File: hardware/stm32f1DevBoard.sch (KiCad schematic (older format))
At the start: 33 parts, among them J1 USB_2, M1 Mounting Hole, M2 Mounting Hole, M3 Mounting Hole, M4 Mounting Hole, P1 JTAG, P2 P20, P3 P20, U1 STM32F102C6, X1 32,768Hz, X2 20MHz

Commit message: using kicadcloud files
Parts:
- C1, C10, C2, C3, C4, C5, C6, C7, C8, C9: symbol CSMALL -> CPsmall
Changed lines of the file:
@@
-EESchema Schematic File Version 2  date Wed 19 Dec 2012 11:05:56 PM EST
-LIBS:stm32f1DevBoard
+EESchema Schematic File Version 2  date Wed 02 Jan 2013 12:15:05 PM EST
+LIBS:userFavorites
 LIBS:power
-LIBS:device
-LIBS:transistors
-LIBS:conn
-LIBS:linear
-LIBS:regul
-LIBS:74xx
-LIBS:cmos4000
-LIBS:adc-dac
-LIBS:memory
-LIBS:xilinx
-LIBS:special
-LIBS:microcontrollers
-LIBS:dsp
-LIBS:microchip
-LIBS:analog_switches
-LIBS:motorola
-LIBS:texas
-LIBS:intel
-LIBS:audio
-LIBS:interface
-LIBS:digital-audio
-LIBS:philips
-LIBS:display
-LIBS:cypress
-LIBS:siliconi
-LIBS:opto
-LIBS:atmel
-LIBS:contrib
-LIBS:valves
-LIBS:stm32f1DevBoard-cache
 EELAYER 27 0
 EELAYER END
@@
 $EndComp
 $Comp
-L CSMALL C10
+L CPsmall C10
 U 1 1 50C94FDC
 P 3900 1750
@@
 $EndComp
 $Comp
-L CSMALL C6
+L CPsmall C6
 U 1 1 50C94FE2
 P 3700 1750
@@
 $EndComp
 $Comp
-L CSMALL C5
+L CPsmall C5
 U 1 1 50C94FE8
 P 3500 1750
@@
 $EndComp
 $Comp
-L CSMALL C2
+L CPsmall C2
 U 1 1 50C94FEE
 P 3300 1750
@@
 $EndComp
 $Comp
-L CSMALL C8
+L CPsmall C8
 U 1 1 50C9642F
 P 3800 2550
@@
 $EndComp
 $Comp
-L CSMALL C3
+L CPsmall C3
 U 1 1 50C96435
 P 3300 2550
@@
 $EndComp
 $Comp
-L CSMALL C9
+L CPsmall C9
 U 1 1 50C9643B
 P 3800 3050
@@
 $EndComp
 $Comp
-L CSMALL C4
+L CPsmall C4
 U 1 1 50C9644B
 P 3300 3050
@@
 $EndComp
 $Comp
-L CSMALL C7
+L CPsmall C7
 U 1 1 50CA0DBA
 P 3750 4250
@@
 $EndComp
 $Comp
-L CSMALL C1
+L CPsmall C1
 U 1 1 50CBFE42
 P 3100 1750

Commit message: updates to schematic
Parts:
- X2: value 20MHz -> 8MHz
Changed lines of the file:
@@
-EESchema Schematic File Version 2  date Thu 17 Jan 2013 09:41:47 PM EST
+EESchema Schematic File Version 2  date Mon 21 Jan 2013 10:28:50 PM EST
 LIBS:userFavorites
 LIBS:power
+LIBS:stm32f1DevBoard-cache
 EELAYER 27 0
 EELAYER END
@@
 Sheet 1 4
 Title ""
-Date "18 jan 2013"
+Date "22 jan 2013"
 Rev ""
 Comp ""
@@
 P 3550 2900
 F 0 "X2" H 3550 3025 60  0000 C CNN
-F 1 "20MHz" H 3550 2775 60  0000 C CNN
+F 1 "8MHz" H 3550 2775 60  0000 C CNN
 	1    3550 2900
 	1    0    0    -1

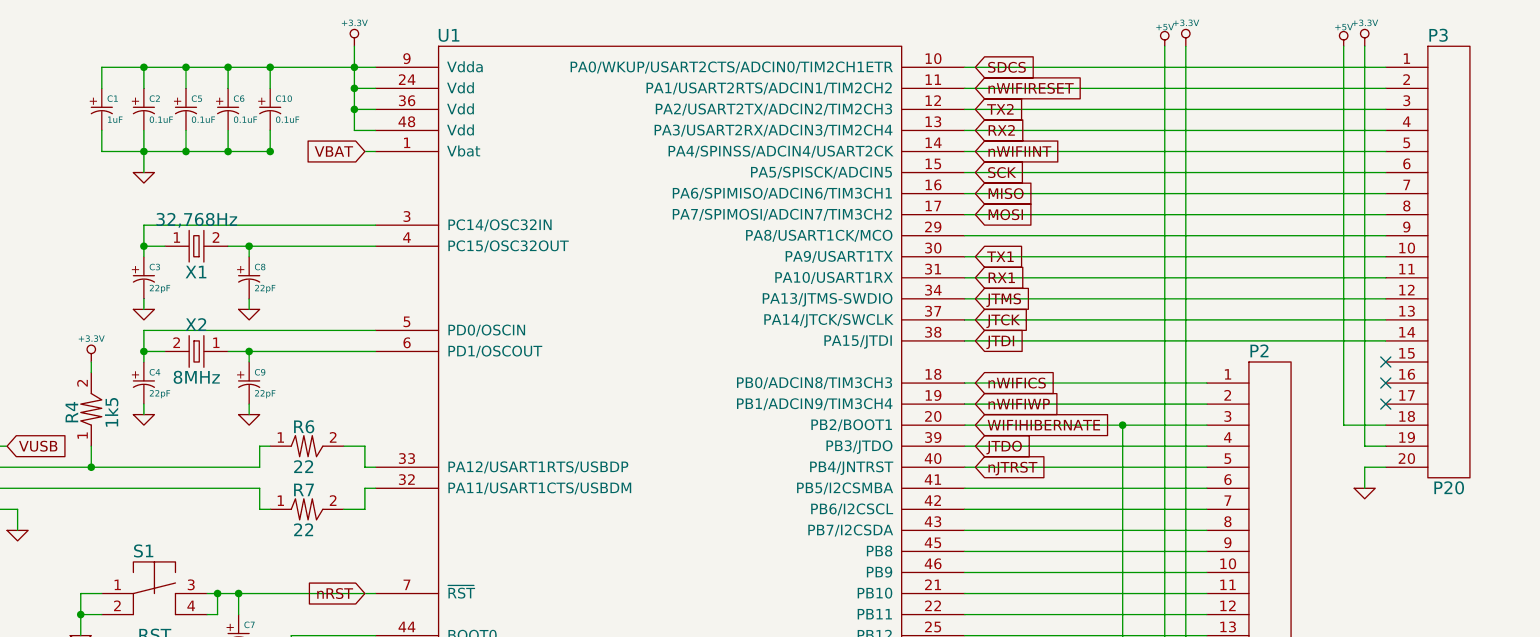
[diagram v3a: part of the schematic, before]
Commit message: fix sdcard
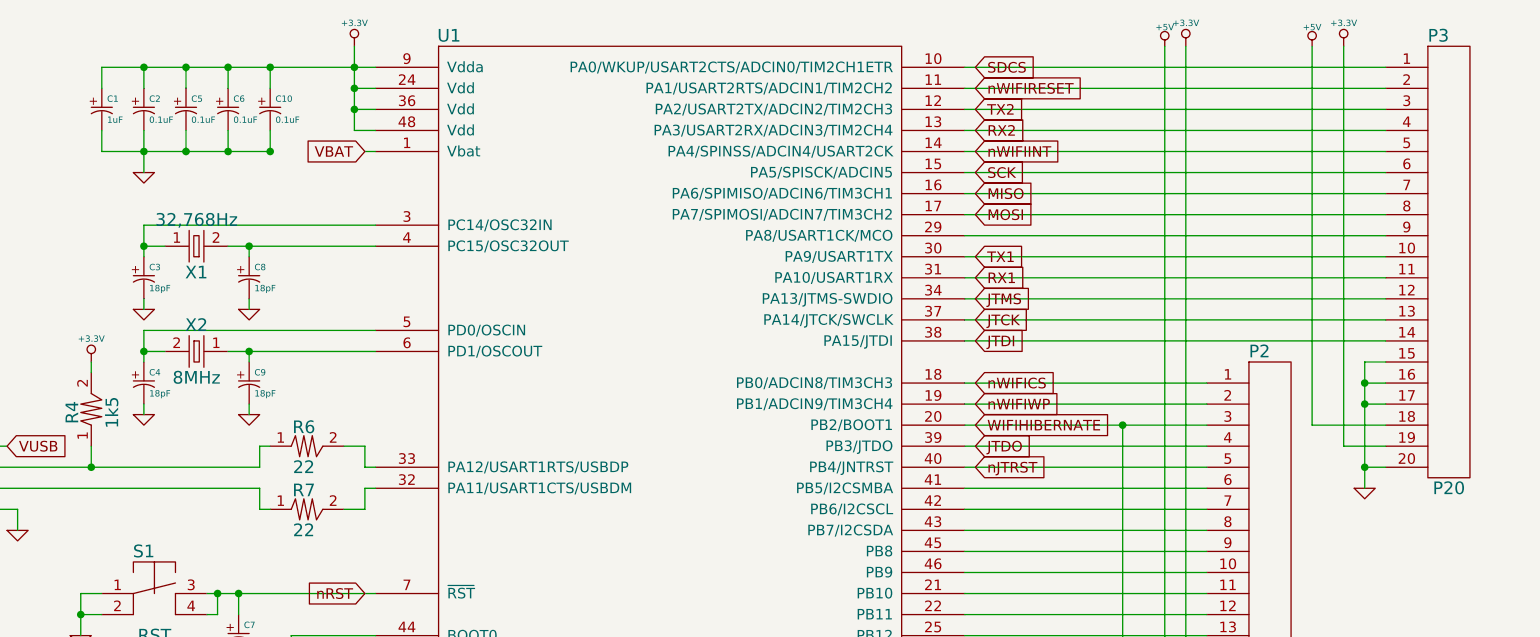
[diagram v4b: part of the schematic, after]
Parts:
- C3, C4, C8, C9: value 22pF -> 18pF
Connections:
- net GND: now also P3.15, P3.16, P3.17
- no-connect marks 3 -> 0
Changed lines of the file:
@@
-EESchema Schematic File Version 2  date Mon 21 Jan 2013 10:28:50 PM EST
+EESchema Schematic File Version 2  date Tue 29 Jan 2013 12:07:46 AM EST
 LIBS:userFavorites
 LIBS:power
@@
 Sheet 1 4
 Title ""
-Date "22 jan 2013"
+Date "29 jan 2013"
 Rev ""
 Comp ""
@@
 $EndDescr
 $Comp
-L +3.3V #PWR18
+L +3.3V #PWR01
 U 1 1 50C949CA
 P 4300 1450
-F 0 "#PWR18" H 4300 1410 30  0001 C CNN
+F 0 "#PWR01" H 4300 1410 30  0001 C CNN
 F 1 "+3.3V" H 4300 1560 30  0000 C CNN
 	1    4300 1450
@@
 $EndComp
 $Comp
-L GND #PWR10
+L GND #PWR02
 U 1 1 50C94D41
 P 3300 2050
-F 0 "#PWR10" H 3300 2050 30  0001 C CNN
+F 0 "#PWR02" H 3300 2050 30  0001 C CNN
 F 1 "GND" H 3300 1980 30  0001 C CNN
 	1    3300 2050
@@
 $EndComp
 $Comp
-L GND #PWR6
+L GND #PWR03
 U 1 1 50C9550D
 P 3000 4250
-F 0 "#PWR6" H 3000 4250 30  0001 C CNN
+F 0 "#PWR03" H 3000 4250 30  0001 C CNN
 F 1 "GND" H 3000 4180 30  0001 C CNN
 	1    3000 4250
@@
 $EndComp
 $Comp
-L GND #PWR19
+L GND #PWR04
 U 1 1 50C95BDE
 P 4300 4850
-F 0 "#PWR19" H 4300 4850 30  0001 C CNN
+F 0 "#PWR04" H 4300 4850 30  0001 C CNN
 F 1 "GND" H 4300 4780 30  0001 C CNN
 	1    4300 4850
@@
 P 3800 2550
 F 0 "C8" H 3825 2600 30  0000 L CNN
-F 1 "22pF" H 3825 2500 30  0000 L CNN
+F 1 "18pF" H 3825 2500 30  0000 L CNN
 	1    3800 2550
 	1    0    0    -1
@@
 P 3300 2550
 F 0 "C3" H 3325 2600 30  0000 L CNN
-F 1 "22pF" H 3325 2500 30  0000 L CNN
+F 1 "18pF" H 3325 2500 30  0000 L CNN
 	1    3300 2550
 	1    0    0    -1
@@
 P 3800 3050
 F 0 "C9" H 3825 3100 30  0000 L CNN
-F 1 "22pF" H 3825 3000 30  0000 L CNN
+F 1 "18pF" H 3825 3000 30  0000 L CNN
 	1    3800 3050
 	1    0    0    -1
@@
 P 3300 3050
 F 0 "C4" H 3325 3100 30  0000 L CNN
-F 1 "22pF" H 3325 3000 30  0000 L CNN
+F 1 "18pF" H 3325 3000 30  0000 L CNN
 	1    3300 3050
 	1    0    0    -1
 $EndComp
 $Comp
-L GND #PWR11
+L GND #PWR05
 U 1 1 50CA07BA
 P 3300 2700
-F 0 "#PWR11" H 3300 2700 30  0001 C CNN
+F 0 "#PWR05" H 3300 2700 30  0001 C CNN
 F 1 "GND" H 3300 2630 30  0001 C CNN
 	1    3300 2700
@@
 $EndComp
 $Comp
-L GND #PWR14
+L GND #PWR06
 U 1 1 50CA07C0
 P 3800 2700
-F 0 "#PWR14" H 3800 2700 30  0001 C CNN
+F 0 "#PWR06" H 3800 2700 30  0001 C CNN
 F 1 "GND" H 3800 2630 30  0001 C CNN
 	1    3800 2700
@@
 $EndComp
 $Comp
-L GND #PWR12
+L GND #PWR07
 U 1 1 50CA07C6
 P 3300 3200
-F 0 "#PWR12" H 3300 3200 30  0001 C CNN
+F 0 "#PWR07" H 3300 3200 30  0001 C CNN
 F 1 "GND" H 3300 3130 30  0001 C CNN
 	1    3300 3200
@@
 $EndComp
 $Comp
-L GND #PWR15
+L GND #PWR08
 U 1 1 50CA07CC
 P 3800 3200
-F 0 "#PWR15" H 3800 3200 30  0001 C CNN
+F 0 "#PWR08" H 3800 3200 30  0001 C CNN
 F 1 "GND" H 3800 3130 30  0001 C CNN
 	1    3800 3200
@@
 $EndComp
 $Comp
-L GND #PWR13
+L GND #PWR09
 U 1 1 50CA0DC0
 P 3750 4450
-F 0 "#PWR13" H 3750 4450 30  0001 C CNN
+F 0 "#PWR09" H 3750 4450 30  0001 C CNN
 F 1 "GND" H 3750 4380 30  0001 C CNN
 	1    3750 4450
@@
 $EndComp
 $Comp
-L GND #PWR8
+L GND #PWR010
 U 1 1 50C9FD3B
 P 3000 5000
-F 0 "#PWR8" H 3000 5000 30  0001 C CNN
+F 0 "#PWR010" H 3000 5000 30  0001 C CNN
 F 1 "GND" H 3000 4930 30  0001 C CNN
 	1    3000 5000
@@
 $EndComp
 $Comp
-L +3.3V #PWR7
+L +3.3V #PWR011
 U 1 1 50C9FD41
 P 3000 4700
-F 0 "#PWR7" H 3000 4660 30  0001 C CNN
+F 0 "#PWR011" H 3000 4660 30  0001 C CNN
 F 1 "+3.3V" H 3000 4810 30  0000 C CNN
 	1    3000 4700
@@
 $EndComp
 $Comp
-L GND #PWR17
+L GND #PWR012
 U 1 1 50CBE59B
 P 3900 6950
-F 0 "#PWR17" H 3900 6950 30  0001 C CNN
+F 0 "#PWR012" H 3900 6950 30  0001 C CNN
 F 1 "GND" H 3900 6880 30  0001 C CNN
 	1    3900 6950
@@
 $EndComp
 $Comp
-L +3.3V #PWR16
+L +3.3V #PWR013
 U 1 1 50CBE85F
 P 3900 5850
-F 0 "#PWR16" H 3900 5810 30  0001 C CNN
+F 0 "#PWR013" H 3900 5810 30  0001 C CNN
 F 1 "+3.3V" H 3900 5960 30  0000 C CNN
 	1    3900 5850
@@
 $EndComp
 $Comp
-L +3.3V #PWR3
+L +3.3V #PWR014
 U 1 1 50CBE8C7
 P 2400 5850
-F 0 "#PWR3" H 2400 5810 30  0001 C CNN
+F 0 "#PWR014" H 2400 5810 30  0001 C CNN
 F 1 "+3.3V" H 2400 5960 30  0000 C CNN
 	1    2400 5850
@@
 $EndComp
 $Comp
-L GND #PWR4
+L GND #PWR015
 U 1 1 50CBE96B
 P 2400 7400
-F 0 "#PWR4" H 2400 7400 30  0001 C CNN
+F 0 "#PWR015" H 2400 7400 30  0001 C CNN
 F 1 "GND" H 2400 7330 30  0001 C CNN
 	1    2400 7400
@@
 $EndComp
 $Comp
-L GND #PWR2
+L GND #PWR016
 U 1 1 50CBE971
 P 2100 7400
-F 0 "#PWR2" H 2100 7400 30  0001 C CNN
+F 0 "#PWR016" H 2100 7400 30  0001 C CNN
 F 1 "GND" H 2100 7330 30  0001 C CNN
 	1    2100 7400
@@
 $EndComp
 $Comp
-L GND #PWR1
+L GND #PWR017
 U 1 1 50CBE977
 P 1800 7400
-F 0 "#PWR1" H 1800 7400 30  0001 C CNN
+F 0 "#PWR017" H 1800 7400 30  0001 C CNN
 F 1 "GND" H 1800 7330 30  0001 C CNN
 	1    1800 7400
@@
 $EndComp
 $Comp
-L GND #PWR5
+L GND #PWR018
 U 1 1 50CC0E79
 P 2700 3750
-F 0 "#PWR5" H 2700 3750 30  0001 C CNN
+F 0 "#PWR018" H 2700 3750 30  0001 C CNN
 F 1 "GND" H 2700 3680 30  0001 C CNN
 	1    2700 3750
@@
 $EndComp
 $Comp
-L +3.3V #PWR9
+L +3.3V #PWR019
 U 1 1 50CC1031
 P 3050 2950
-F 0 "#PWR9" H 3050 2910 30  0001 C CNN
+F 0 "#PWR019" H 3050 2910 30  0001 C CNN
 F 1 "+3.3V" H 3050 3060 30  0000 C CNN
 	1    3050 2950
@@
 	7300 4650 8350 4650
 $Comp
-L GND #PWR26
+L GND #PWR020
 U 1 1 50CD9603
 P 9100 3550
-F 0 "#PWR26" H 9100 3550 30  0001 C CNN
+F 0 "#PWR020" H 9100 3550 30  0001 C CNN
 F 1 "GND" H 9100 3480 30  0001 C CNN
 	1    9100 3550
@@
 $EndComp
 $Comp
-L GND #PWR23
+L GND #PWR021
 U 1 1 50CD9609
 P 8250 5050
-F 0 "#PWR23" H 8250 5050 30  0001 C CNN
+F 0 "#PWR021" H 8250 5050 30  0001 C CNN
 F 1 "GND" H 8250 4980 30  0001 C CNN
 	1    8250 5050
@@
 	9200 3450 9100 3450
 Wire Wire Line
-	9100 3450 9100 3550
-$Comp
-L +3.3V #PWR25
+	9100 2950 9100 3550
+$Comp
+L +3.3V #PWR022
 U 1 1 50CD9878
-P 9100 1450
-F 0 "#PWR25" H 9100 1410 30  0001 C CNN
-F 1 "+3.3V" H 9100 1560 30  0000 C CNN
-	1    9100 1450
-	1    0    0    -1
-$EndComp
-$Comp
-L +3.3V #PWR22
+P 9000 1450
+F 0 "#PWR022" H 9000 1410 30  0001 C CNN
+F 1 "+3.3V" H 9000 1560 30  0000 C CNN
+	1    9000 1450
+	1    0    0    -1
+$EndComp
+$Comp
+L +3.3V #PWR023
 U 1 1 50CD987E
 P 8250 1450
-F 0 "#PWR22" H 8250 1410 30  0001 C CNN
+F 0 "#PWR023" H 8250 1410 30  0001 C CNN
 F 1 "+3.3V" H 8250 1560 30  0000 C CNN
 	1    8250 1450
@@
 Wire Wire Line
 	8250 4850 8250 1450
-Wire Wire Line
-	9200 3350 9100 3350
-Wire Wire Line
-	9100 3350 9100 1450
-$Comp
-L +5V #PWR21
+$Comp
+L +5V #PWR024
 U 1 1 50CD9B00
 P 8150 1450
-F 0 "#PWR21" H 8150 1540 20  0001 C CNN
+F 0 "#PWR024" H 8150 1540 20  0001 C CNN
 F 1 "+5V" H 8150 1540 30  0000 C CNN
 	1    8150 1450
@@
 $EndComp
 $Comp
-L GND #PWR20
+L GND #PWR025
 U 1 1 50CDC19E
 P 7950 5250
-F 0 "#PWR20" H 7950 5250 30  0001 C CNN
+F 0 "#PWR025" H 7950 5250 30  0001 C CNN
 F 1 "GND" H 7950 5180 30  0001 C CNN
 	1    7950 5250
@@
 JTDI
 $Comp
-L +5V #PWR24
+L +5V #PWR026
 U 1 1 50CE57F4
-P 9000 1450
-F 0 "#PWR24" H 9000 1540 20  0001 C CNN
-F 1 "+5V" H 9000 1540 30  0000 C CNN
-	1    9000 1450
-	1    0    0    -1
-$EndComp
-Wire Wire Line
-	9200 3250 9000 3250
-Wire Wire Line
-	9000 3250 9000 1450
-NoConn ~ 9200 2950
-NoConn ~ 9200 3050
-NoConn ~ 9200 3150
+P 8850 1450
+F 0 "#PWR026" H 8850 1540 20  0001 C CNN
+F 1 "+5V" H 8850 1540 30  0000 C CNN
+	1    8850 1450
+	1    0    0    -1
+$EndComp
 Wire Wire Line
 	4350 1950 4400 1950
@@
 Wire Wire Line
 	2450 3350 2650 3350
+Wire Wire Line
+	9200 3250 8850 3250
+Wire Wire Line
+	8850 3250 8850 1450
+Wire Wire Line
+	9200 3350 9000 3350
+Wire Wire Line
+	9000 3350 9000 1450
+Wire Wire Line
+	9200 2950 9100 2950
+Connection ~ 9100 3450
+Wire Wire Line
+	9200 3050 9100 3050
+Connection ~ 9100 3050
+Wire Wire Line
+	9200 3150 9100 3150
+Connection ~ 9100 3150
 $EndSCHEMATC

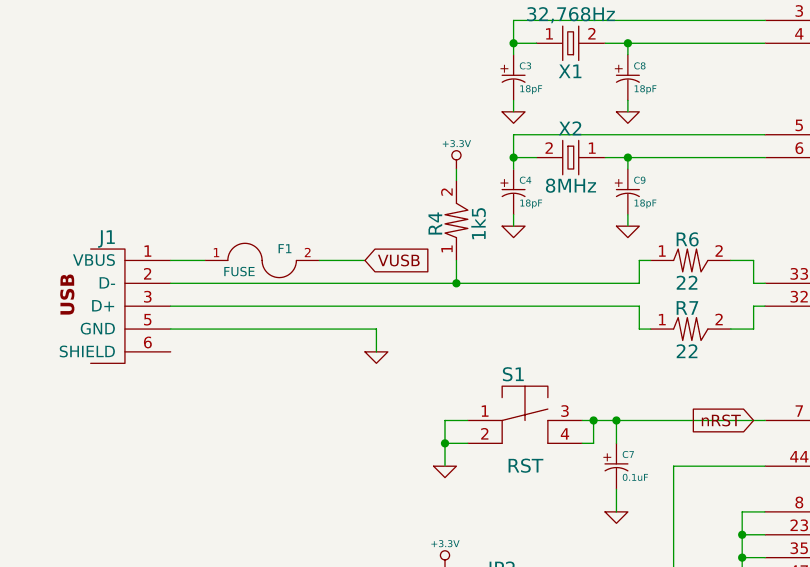
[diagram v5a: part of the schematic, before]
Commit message: usb renumber
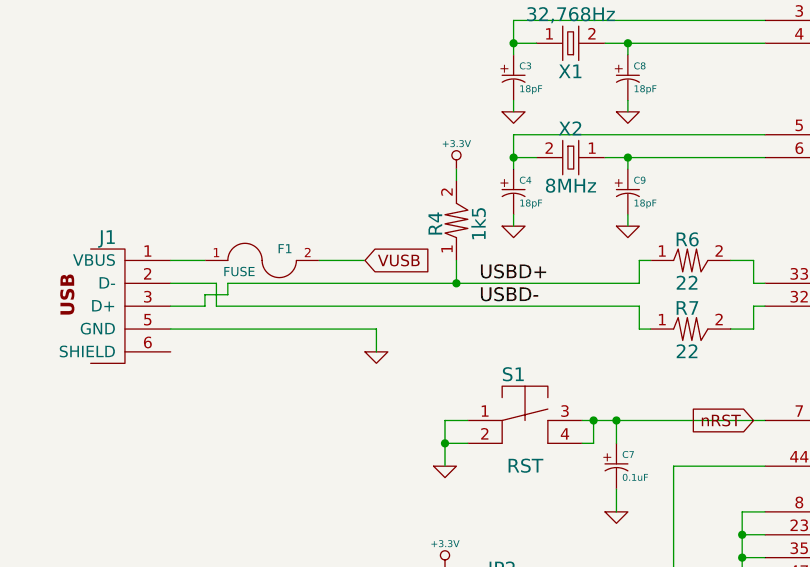
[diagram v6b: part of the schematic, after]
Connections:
- net USBD+: now reaches R4.1, R6.1
- net USBD+: now also J1.3 (D+); no longer J1.2 (D-)
- net USBD-: now reaches R7.1
- net USBD-: now also J1.2 (D-); no longer J1.3 (D+)
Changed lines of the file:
@@
-EESchema Schematic File Version 2  date Tue 29 Jan 2013 11:51:38 AM EST
+EESchema Schematic File Version 2  date Thu 31 Jan 2013 11:01:55 PM EST
 LIBS:userFavorites
 LIBS:power
@@
 Sheet 1 4
 Title ""
-Date "29 jan 2013"
+Date "1 feb 2013"
 Rev ""
 Comp ""
@@
 P 1600 3500
 F 0 "J1" H 1525 3750 60  0000 C CNN
-F 1 "USB_2" H 1650 3200 60  0001 C CNN
+F 1 "USB_2" H 1650 3150 60  0001 C CNN
 F 4 "VCC" H 1925 3650 50  0001 C CNN "VCC"
 F 5 "D+" H 1900 3550 50  0001 C CNN "Data+"
@@
 	3850 3350 3850 3450
 Wire Wire Line
-	3850 3450 1800 3450
-Wire Wire Line
 	3900 3650 3850 3650
 Wire Wire Line
 	3850 3650 3850 3550
-Wire Wire Line
-	3850 3550 1800 3550
 Wire Wire Line
 	1800 3650 2700 3650
@@
 	9200 3150 9100 3150
 Connection ~ 9100 3150
+Wire Wire Line
+	1800 3450 2000 3450
+Wire Wire Line
+	2000 3450 2000 3550
+Wire Wire Line
+	2000 3550 3850 3550
+Wire Wire Line
+	1800 3550 1950 3550
+Wire Wire Line
+	1950 3550 1950 3500
+Wire Wire Line
+	1950 3500 2050 3500
+Wire Wire Line
+	2050 3500 2050 3450
+Wire Wire Line
+	2050 3450 3850 3450
+Text Label 3150 3550 0    60   ~ 0
+USBD-
+Text Label 3150 3450 0    60   ~ 0
+USBD+
 $EndSCHEMATC

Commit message: update hardware
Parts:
- removed JP1: JTAG_ENABLE, symbol JUMPER_2X1
- added C19, C20: 47pF, symbol CPsmall
- added D3: DIODESCH, symbol DIODESCH
- added Q2: MOSFET-P, symbol MOSFET-P
- added R20: 10k, symbol R
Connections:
- net +3.3V: now also Q2.3, R20.2; no longer R4.2
- net GND: now also C19.2, C20.2
- net USBD+: no longer R4.1
- net VUSB: now also D3.2 (K); no longer F1.2
- net nRST: now also P1.15 (~SRST)
- net at R7.2, U1.32 (PA11/USART1CTS/USBDM): now also C20.1
- net at R6.2, U1.33 (PA12/USART1RTS/USBDP): now also R4.1, C19.1
- net USBDISC: now reaches P2.10, U1.46 (PB9)
- net USBDISC: now also Q2.1, R20.1
- new net: Q2.2, R4.2
- new net: D3.1 (A), F1.2
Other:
- moved on the sheet: C1, C10, C2, C3, C4, C5, C6, C7, C8, C9, F1, J1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
